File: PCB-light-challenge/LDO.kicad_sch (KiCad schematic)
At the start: 2 parts

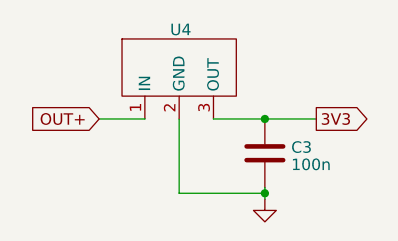
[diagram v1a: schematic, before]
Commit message: EDS protection en fuse toegevoegd
we moeten nog wel footprints checken
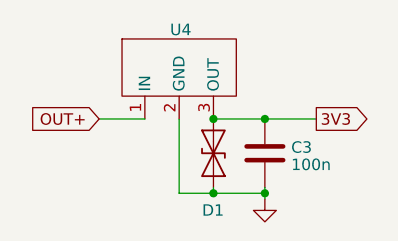
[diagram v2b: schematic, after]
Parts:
- added D1: ESD9B3.3ST5G, Diode_SMD:D_SOD-323_HandSoldering, symbol Diode:ESD9B3.3ST5G
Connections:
- net 3V3: now also D1.2 (A2)
- net GND: now also D1.1 (A1)
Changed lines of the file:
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@@
     (company "HHS Living Labs")
+  )
+  (junction (at 100.965 64.77) (diameter 0) (color 0 0 0 0)
   )
   (junction (at 106.68 64.77) (diameter 0) (color 0 0 0 0)
@@
   (junction (at 106.68 73.025) (diameter 0) (color 0 0 0 0)
   )
+  (junction (at 100.965 73.025) (diameter 0) (color 0 0 0 0)
+  )
   (wire (pts (xy 106.68 73.025) (xy 106.68 73.66))
     (stroke (width 0) (type default))
   )
-  (wire (pts (xy 97.155 73.025) (xy 106.68 73.025))
+  (wire (pts (xy 100.965 73.025) (xy 106.68 73.025))
+    (stroke (width 0) (type default))
+  )
+  (wire (pts (xy 97.155 73.025) (xy 100.965 73.025))
     (stroke (width 0) (type default))
   )
@@
   )
   (wire (pts (xy 100.965 64.77) (xy 106.68 64.77))
+    (stroke (width 0) (type default))
+  )
+  (wire (pts (xy 100.965 72.39) (xy 100.965 73.025))
     (stroke (width 0) (type default))
   )
@@
         )
       )
+    )
+  )
+  (symbol (lib_id "Diode:ESD9B3.3ST5G") (at 100.965 68.58 90) (unit 1)
+    (in_bom yes) (on_board yes) (dnp no)
+    (property "Reference" "D1" (at 99.695 74.93 90)
+      (effects (font (size 1.27 1.27)) (justify right))
+    )
+    (property "Value" "ESD9B3.3ST5G" (at 104.14 69.85 90)
+      (effects (font (size 1.27 1.27)) (justify right) hide)
+    )
+    (property "Footprint" "Diode_SMD:D_SOD-323_HandSoldering" (at 100.965 68.58 0)
+      (effects (font (size 1.27 1.27)) hide)
+    )
+    (property "Datasheet" "https://www.onsemi.com/pub/Collateral/ESD9B-D.PDF" (at 100.965 68.58 0)
+      (effects (font (size 1.27 1.27)) hide)
+    )
+    (pin "1")
+    (pin "2")
+    (instances
+      (project "PCB-light-challenge"
+        (path "/35573e8f-7834-430c-81d2-239f316c7834/1ee2b17a-9b36-4608-9d61-b871128bc979"
+          (reference "D1") (unit 1)
+        )
+        (path "/35573e8f-7834-430c-81d2-239f316c7834/a8982b6c-f9f4-4ae9-b882-3fbabc855f32"
+          (reference "D2") (unit 1)
+        )
+      )

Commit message: PCB 80% af
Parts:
- C3: footprint (none) -> Capacitor_SMD:C_0603_1608Metric
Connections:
- net OUT+ renamed P+
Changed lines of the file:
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@@
     (stroke (width 0) (type default))
-  )
-  (global_label "OUT+" (shape input) (at 88.265 64.77 180) (fields_autoplaced)
-    (effects (font (size 1.27 1.27)) (justify right))
-    (property "Intersheetrefs" "${INTERSHEET_REFS}" (at 80.1582 64.77 0)
-      (effects (font (size 1.27 1.27)) (justify right) hide)
-    )
   )
   (global_label "3V3" (shape output) (at 112.395 64.77 0) (fields_autoplaced)
@@
     (property "Intersheetrefs" "${INTERSHEET_REFS}" (at 118.8084 64.77 0)
       (effects (font (size 1.27 1.27)) (justify left) hide)
+    )
+  )
+  (global_label "P+" (shape input) (at 88.2904 64.77 180) (fields_autoplaced)
+    (effects (font (size 1.27 1.27)) (justify right))
+    (property "Intersheetrefs" "${INTERSHEET_REFS}" (at 82.5422 64.77 0)
+      (effects (font (size 1.27 1.27)) (justify right) hide)
     )
   )
@@
       (effects (font (size 1.27 1.27)) (justify left))
     )
-    (property "Footprint" "" (at 107.6452 72.39 0)
+    (property "Footprint" "Capacitor_SMD:C_0603_1608Metric" (at 107.6452 72.39 0)
       (effects (font (size 1.27 1.27)) hide)
     )
